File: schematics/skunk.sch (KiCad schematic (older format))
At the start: 30 parts

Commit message: Added regulator to schematic
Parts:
- added C?: C, symbol C
- added C?: CP1, symbol CP1
- added R? (x2): R, symbol R
- added U?: LM317, symbol LM317
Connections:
- net labels added: +18V, 0V_SENSE
- net labels removed: 0V SENSE
- wire segments 126 -> 142

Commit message: Enlarged schem paper size, replace 317 and 2nd batt with boost switcher
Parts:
- removed BT?: 12V SLAB BAT2, symbol BATTERY
- removed C?: C, symbol C
- removed C?: CP1, symbol CP1
- removed P? (x2): CONN_BAT_2, symbol CONN_2
- removed R? (x2): R, symbol R
- removed U?: LM317, symbol LM317
- BT?: value 12V SLAB BAT1 -> BAT1
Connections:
- net labels added: +16V, Vin, Vout
- net labels removed: +18V, +24V
- wire segments 142 -> 130
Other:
- note added: "BOOST SWITCHER\nMODULE"
- moved on the sheet: J?, K?, P?, RV?, SP?, SW?

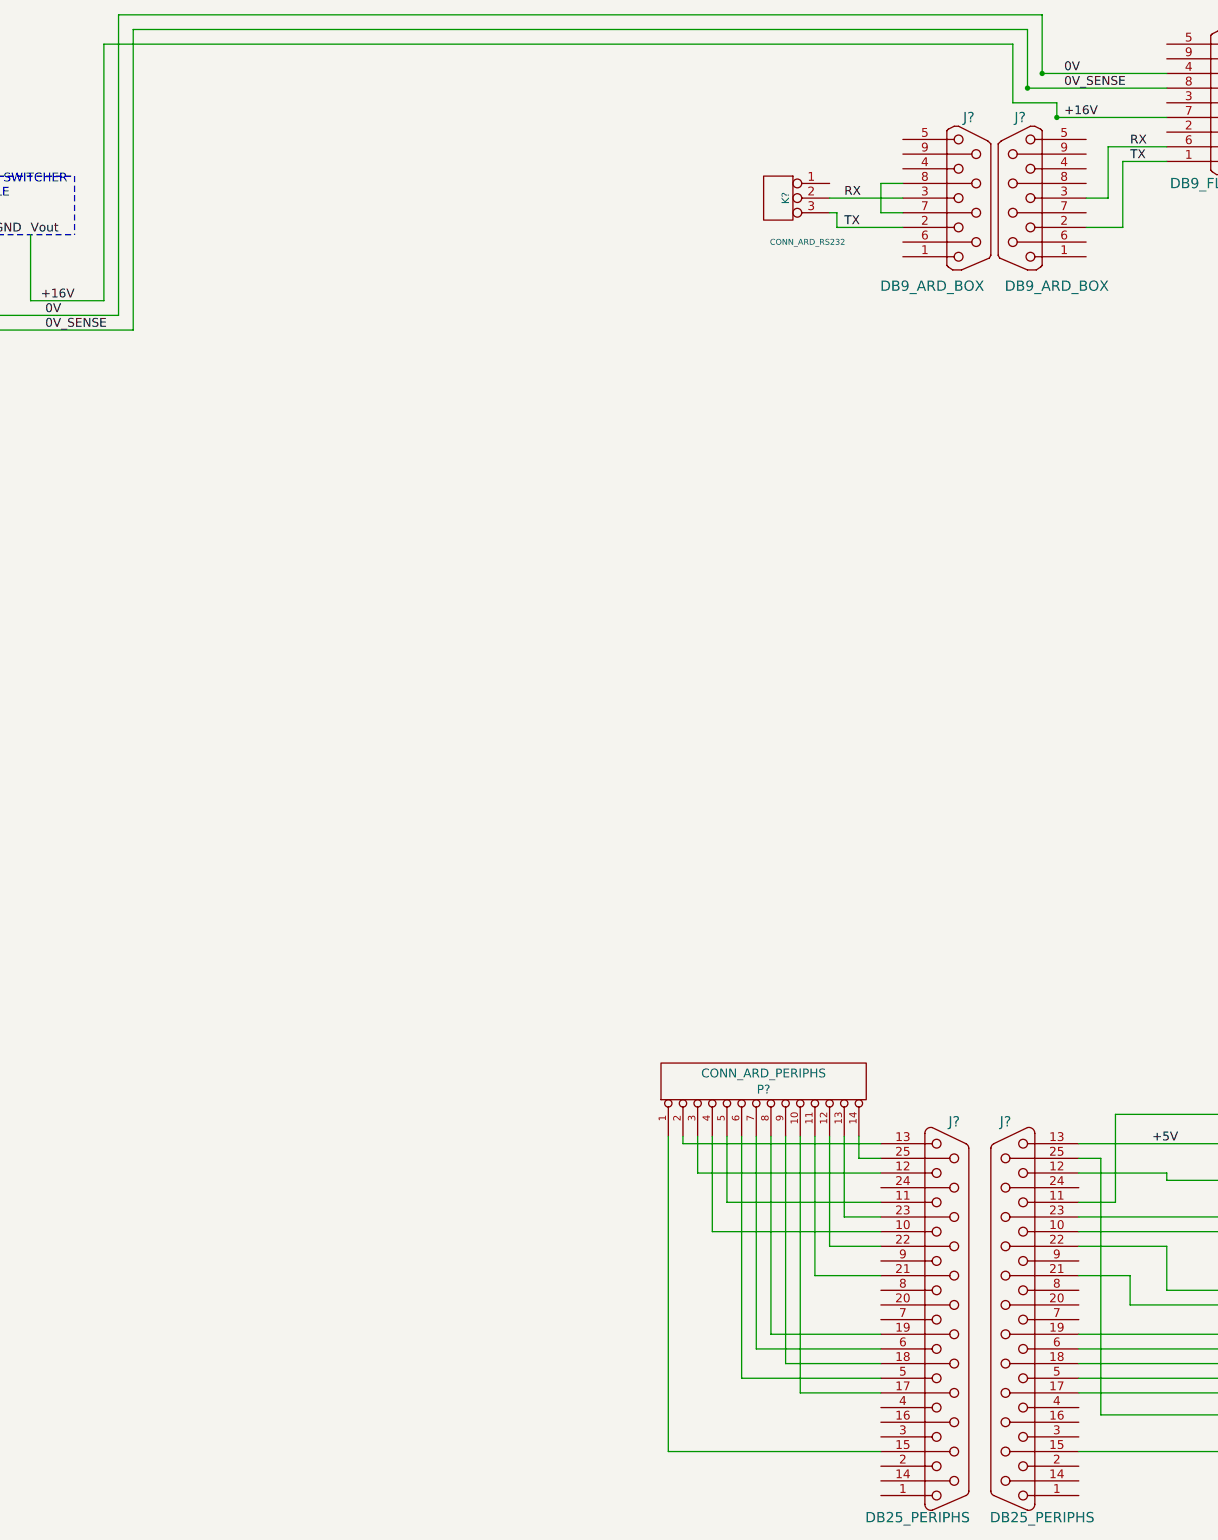
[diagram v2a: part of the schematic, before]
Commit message: Added DB25 cable to schem
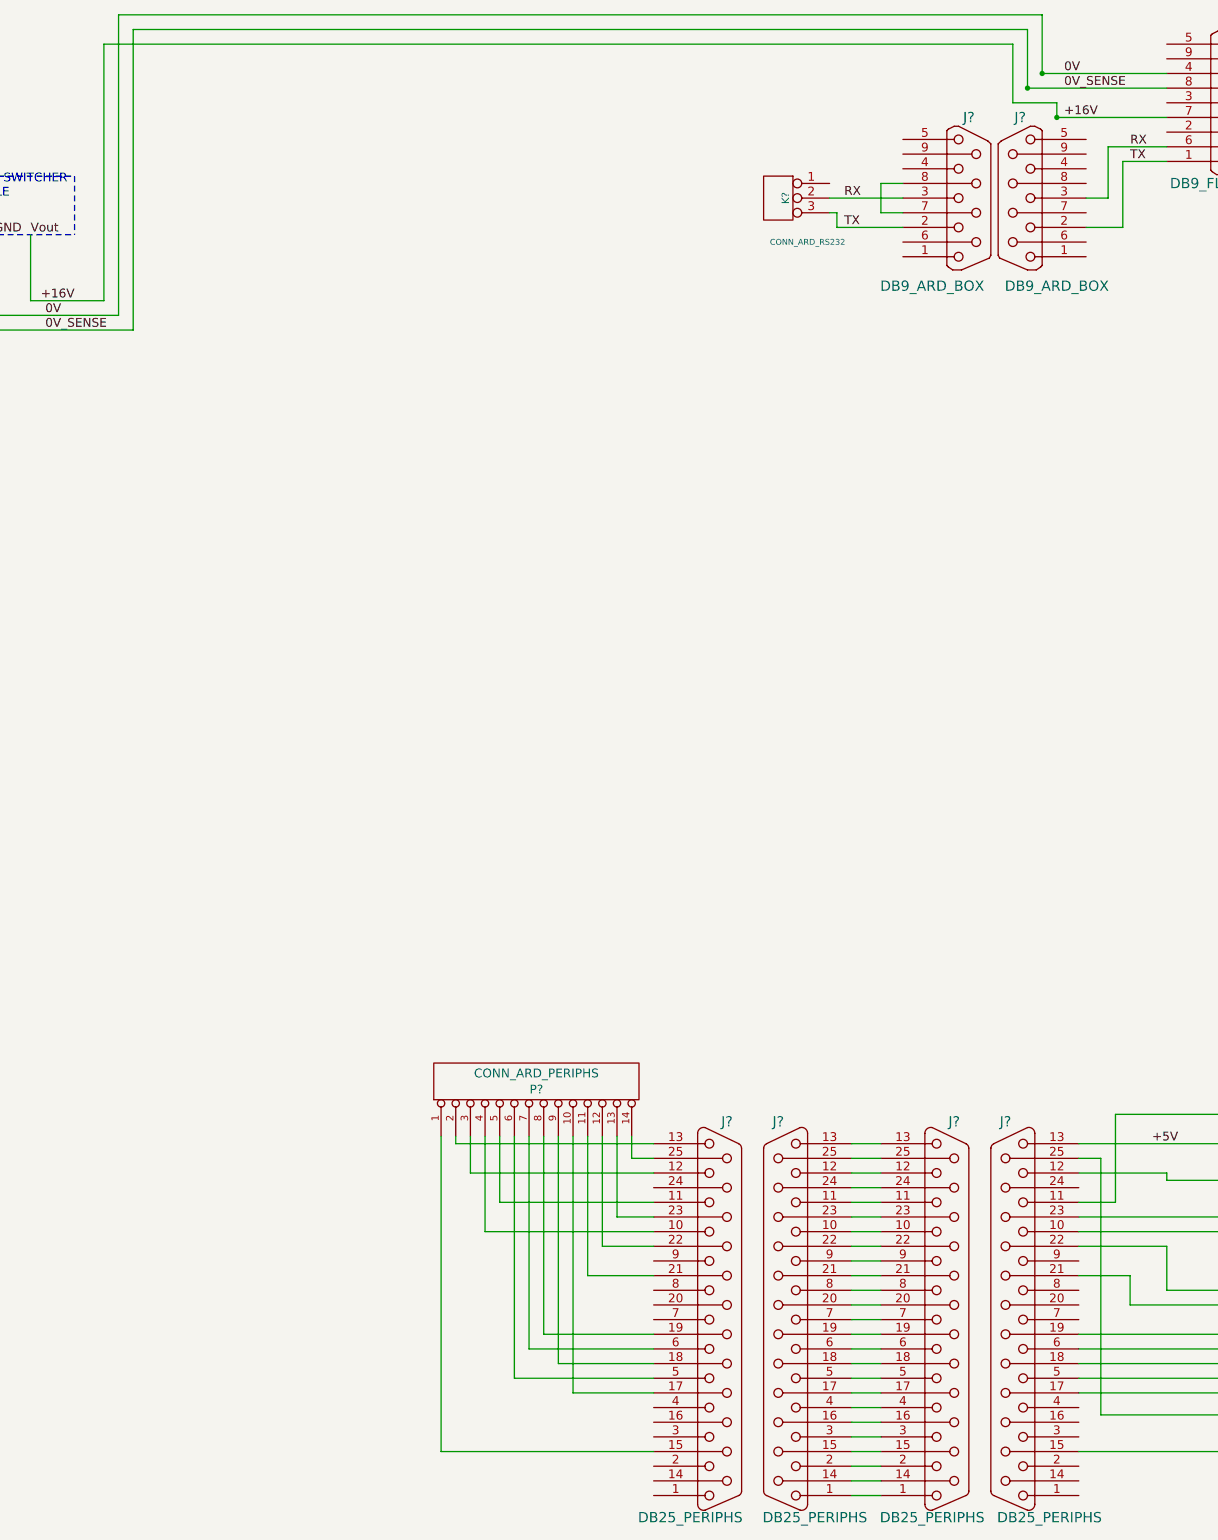
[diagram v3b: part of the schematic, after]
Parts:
- added J? (x2): DB25_PERIPHS, symbol DB25
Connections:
- new net: J?.1, J?.1
- new net: J?.10, J?.10
- new net: J?.11, J?.11
- new net: J?.12, J?.12
- new net: J?.13, J?.13
- new net: J?.14 (P14), J?.14 (P14)
- new net: J?.15 (P15), J?.15 (P15)
- new net: J?.16 (P16), J?.16 (P16)
- new net: J?.17 (P17), J?.17 (P17)
- new net: J?.18 (P18), J?.18 (P18)
- new net: J?.19 (P19), J?.19 (P19)
- new net: J?.2, J?.2
- new net: J?.20 (P20), J?.20 (P20)
- new net: J?.21 (P21), J?.21 (P21)
- new net: J?.22 (P22), J?.22 (P22)
- new net: J?.23 (P23), J?.23 (P23)
- new net: J?.24 (P24), J?.24 (P24)
- new net: J?.25 (P25), J?.25 (P25)
- new net: J?.3, J?.3
- new net: J?.4, J?.4
- new net: J?.5, J?.5
- new net: J?.6, J?.6
- new net: J?.7, J?.7
- new net: J?.8, J?.8
- new net: J?.9, J?.9
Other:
- moved on the sheet: J?, P?
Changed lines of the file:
@@
-EESchema Schematic File Version 2  date Fri 05 Oct 2012 14:48:07 BST
+EESchema Schematic File Version 2  date Fri 05 Oct 2012 14:57:27 BST
 LIBS:power
 LIBS:device
@@
 	9500 1250 9500 1150
 Wire Wire Line
-	9200 1150 9500 1150
-Wire Wire Line
-	9200 750  9200 1150
+	9500 1150 9200 1150
+Wire Wire Line
+	9200 1150 9200 750
 Wire Wire Line
 	10250 1050 9300 1050
@@
 	10250 950  9400 950
 Wire Wire Line
-	7650 8200 7650 9750
-Wire Wire Line
-	7450 8200 7450 9650
-Wire Wire Line
-	6850 8200 6850 10350
-Wire Wire Line
-	7150 8200 7150 8850
-Wire Wire Line
-	6950 8200 6950 8250
-Wire Wire Line
-	7850 8200 7850 9150
-Wire Wire Line
-	8300 8350 8150 8350
-Wire Wire Line
-	8150 8350 8150 8200
+	6100 8200 6100 9750
+Wire Wire Line
+	5900 8200 5900 9650
+Wire Wire Line
+	5300 8200 5300 10350
+Wire Wire Line
+	5600 8200 5600 8850
+Wire Wire Line
+	5400 8200 5400 8250
+Wire Wire Line
+	6300 8200 6300 9150
+Wire Wire Line
+	6750 8350 6600 8350
+Wire Wire Line
+	6600 8350 6600 8200
 Wire Wire Line
 	900  2900 1650 2900
@@
 	1300 2700 3200 2700
 Wire Wire Line
-	7650 9750 8300 9750
-Wire Wire Line
-	8300 9550 7550 9550
-Wire Wire Line
-	8300 8950 7950 8950
-Wire Wire Line
-	8300 8750 8050 8750
-Wire Wire Line
-	8300 8450 7050 8450
-Wire Wire Line
-	6950 8250 8300 8250
-Wire Wire Line
-	6850 10350 8300 10350
+	6100 9750 6750 9750
+Wire Wire Line
+	6750 9550 6000 9550
+Wire Wire Line
+	6750 8950 6400 8950
+Wire Wire Line
+	6750 8750 6500 8750
+Wire Wire Line
+	6750 8450 5500 8450
+Wire Wire Line
+	5400 8250 6750 8250
+Wire Wire Line
+	5300 10350 6750 10350
 Wire Wire Line
 	8450 2000 8000 2000
@@
 	10250 1450 9850 1450
 Wire Wire Line
-	8300 9950 7750 9950
-Wire Wire Line
-	8300 8650 7250 8650
-Wire Wire Line
-	7150 8850 8300 8850
-Wire Wire Line
-	7850 9150 8300 9150
-Wire Wire Line
-	7450 9650 8300 9650
-Wire Wire Line
-	8300 9850 7350 9850
+	6750 9950 6200 9950
+Wire Wire Line
+	6750 8650 5700 8650
+Wire Wire Line
+	5600 8850 6750 8850
+Wire Wire Line
+	6300 9150 6750 9150
+Wire Wire Line
+	5900 9650 6750 9650
+Wire Wire Line
+	6750 9850 5800 9850
 Wire Wire Line
 	1300 2600 3100 2600
@@
 	850  2550 850  3200
 Wire Wire Line
-	8050 8750 8050 8200
-Wire Wire Line
-	7950 8950 7950 8200
-Wire Wire Line
-	7050 8450 7050 8200
-Wire Wire Line
-	7250 8650 7250 8200
-Wire Wire Line
-	7350 9850 7350 8200
-Wire Wire Line
-	7550 9550 7550 8200
-Wire Wire Line
-	7750 9950 7750 8200
+	6500 8750 6500 8200
+Wire Wire Line
+	6400 8950 6400 8200
+Wire Wire Line
+	5500 8450 5500 8200
+Wire Wire Line
+	5700 8650 5700 8200
+Wire Wire Line
+	5800 9850 5800 8200
+Wire Wire Line
+	6000 9550 6000 8200
+Wire Wire Line
+	6200 9950 6200 8200
 Wire Wire Line
 	3100 2600 3100 550
@@
 P 9200 9450
 F 0 "J?" H 9250 10800 70  0000 C CNN
-F 1 "DB25_PERIPHS" H 9000 8100 70  0000 C CNN
+F 1 "DB25_PERIPHS" H 8950 8100 70  0000 C CNN
 	1    9200 9450
 	-1   0    0    -1
@@
 L DB25 J?
 U 1 1 50636AAF
-P 8750 9450
-F 0 "J?" H 8800 10800 70  0000 C CNN
-F 1 "DB25_PERIPHS" H 8550 8100 70  0000 C CNN
-	1    8750 9450
+P 7200 9450
+F 0 "J?" H 7250 10800 70  0000 C CNN
+F 1 "DB25_PERIPHS" H 7000 8100 70  0000 C CNN
+	1    7200 9450
 	1    0    0    -1
 $EndComp
@@
 L CONN_14 P?
 U 1 1 50636A9D
-P 7500 7850
-F 0 "P?" V 7470 7850 60  0000 C CNN
-F 1 "CONN_ARD_PERIPHS" V 7580 7850 60  0000 C CNN
-	1    7500 7850
+P 5950 7850
+F 0 "P?" V 5920 7850 60  0000 C CNN
+F 1 "CONN_ARD_PERIPHS" V 6030 7850 60  0000 C CNN
+	1    5950 7850
 	0    -1   -1   0
 $EndComp
@@
 	2800 1650 2800 2050
 Wire Wire Line
-	3000 750  9200 750
+	9200 750  3000 750
+$Comp
+L DB25 J?
+U 1 1 506EE73C
+P 8750 9450
+F 0 "J?" H 8800 10800 70  0000 C CNN
+F 1 "DB25_PERIPHS" H 8650 8100 70  0000 C CNN
+	1    8750 9450
+	1    0    0    -1
+$EndComp
+$Comp
+L DB25 J?
+U 1 1 506EE74B
+P 7650 9450
+F 0 "J?" H 7700 10800 70  0000 C CNN
+F 1 "DB25_PERIPHS" H 7450 8100 70  0000 C CNN
+	1    7650 9450
+	-1   0    0    -1
+$EndComp
+Wire Wire Line
+	8100 8250 8300 8250
+Wire Wire Line
+	8300 8350 8100 8350
+Wire Wire Line
+	8100 8450 8300 8450
+Wire Wire Line
+	8300 8550 8100 8550
+Wire Wire Line
+	8100 8650 8300 8650
+Wire Wire Line
+	8300 8750 8100 8750
+Wire Wire Line
+	8100 8850 8300 8850
+Wire Wire Line
+	8300 8950 8100 8950
+Wire Wire Line
+	8100 9050 8300 9050
+Wire Wire Line
+	8300 9150 8100 9150
+Wire Wire Line
+	8100 9250 8300 9250
+Wire Wire Line
+	8300 9350 8100 9350
+Wire Wire Line
+	8100 9450 8300 9450
+Wire Wire Line
+	8300 9550 8100 9550
+Wire Wire Line
+	8100 9650 8300 9650
+Wire Wire Line
+	8300 9750 8100 9750
+Wire Wire Line
+	8100 9850 8300 9850
+Wire Wire Line
+	8300 9950 8100 9950
+Wire Wire Line
+	8100 10050 8300 10050
+Wire Wire Line
+	8300 10150 8100 10150
+Wire Wire Line
+	8100 10250 8300 10250
+Wire Wire Line
+	8300 10350 8100 10350
+Wire Wire Line
+	8100 10450 8300 10450
+Wire Wire Line
+	8300 10550 8100 10550
+Wire Wire Line
+	8100 10650 8300 10650
 $EndSCHEMATC

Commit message: Added crowbar circuit and idiot diode to schem
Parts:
- added C?: 100nF, symbol C
- added C?: 47nF, symbol C
- added D?: 20V, symbol ZENER
- added D?: DIODE, symbol DIODE
- added F?: FUSE 2A, symbol FUSE
- added F?: FUSE 1A, symbol FUSE
- added R?: 1k, symbol R
- added T?: THYRISTOR, symbol THYRISTOR
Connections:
- net +12V: now also D?.2 (K), F?.2; no longer P?.2 (PM)
- net +16V: now also C?.1, D?.2 (K), F?.1, F?.2, T?.A
- net GND: now also C?.2, C?.2, D?.1 (A), R?.2, T?.K
- new net: F?.1, P?.2 (PM)
- new net: C?.1, D?.1 (A), R?.1, T?.G
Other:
- note added: "IDIOT\nDIODE"
- note added: "OVERVOLTAGE CROWBAR"
- note added: "POWER INPUT\n"
- moved on the sheet: BT?, J?, P?
